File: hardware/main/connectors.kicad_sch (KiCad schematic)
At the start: 0 parts

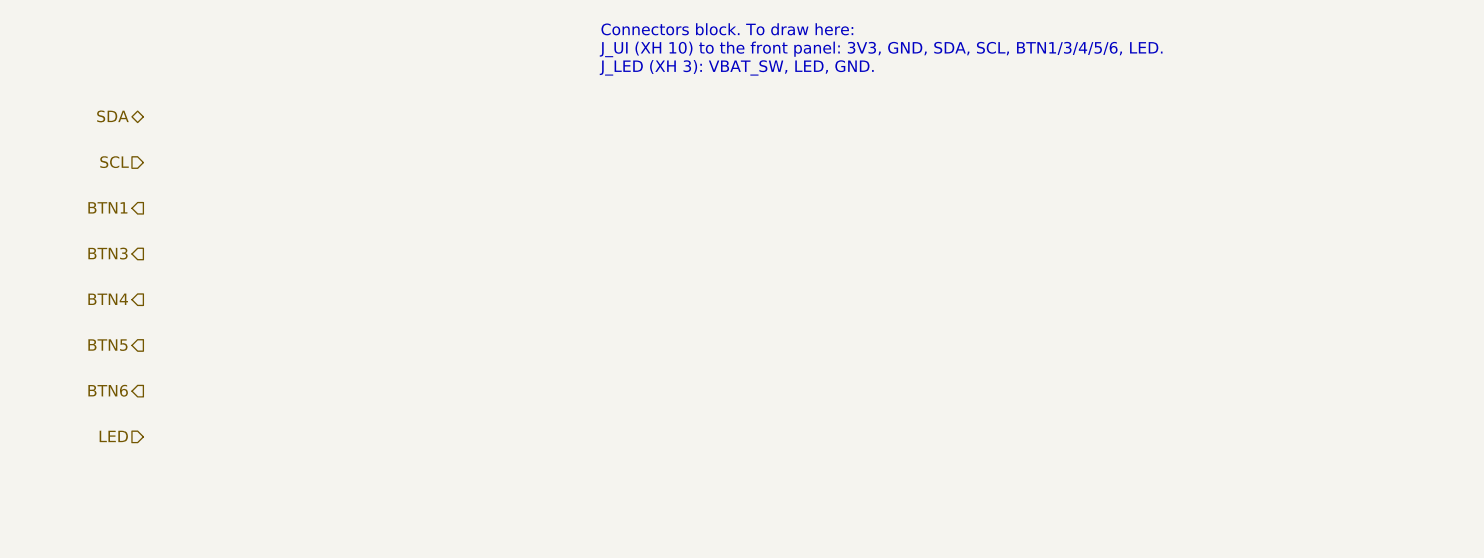
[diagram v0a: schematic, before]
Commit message: hardware: footprints for every part, LCSC library, real A1S pin plan
- lib/lcsc: ESP32-A1S, NS4150B, FS8205A, MSK12C02, PJ-320D imported
  from LCSC with easyeda2kicad (3D paths fixed, NPTH pegs, A1S antenna
  keepout and courtyard), registered in all three projects.
- Parts table with footprint and LCSC number in hardware/README.md.
- The A1S keeps the codec's I2C/I2S inside: display moves to the
  ST7789's pins 14/13/15/22 (SPI or I2C), LED to 12, CHRG/STDBY to 4/2
  through BAT54W. J_SW and J_CHG for an off-board switch and charge LEDs.
- Block sheets use the module's real outputs (HPOUTL/R, SPOLP/N, SPORP/N).

Co-Authored-By: Claude Opus 5.5 <noreply@anthropic.com>
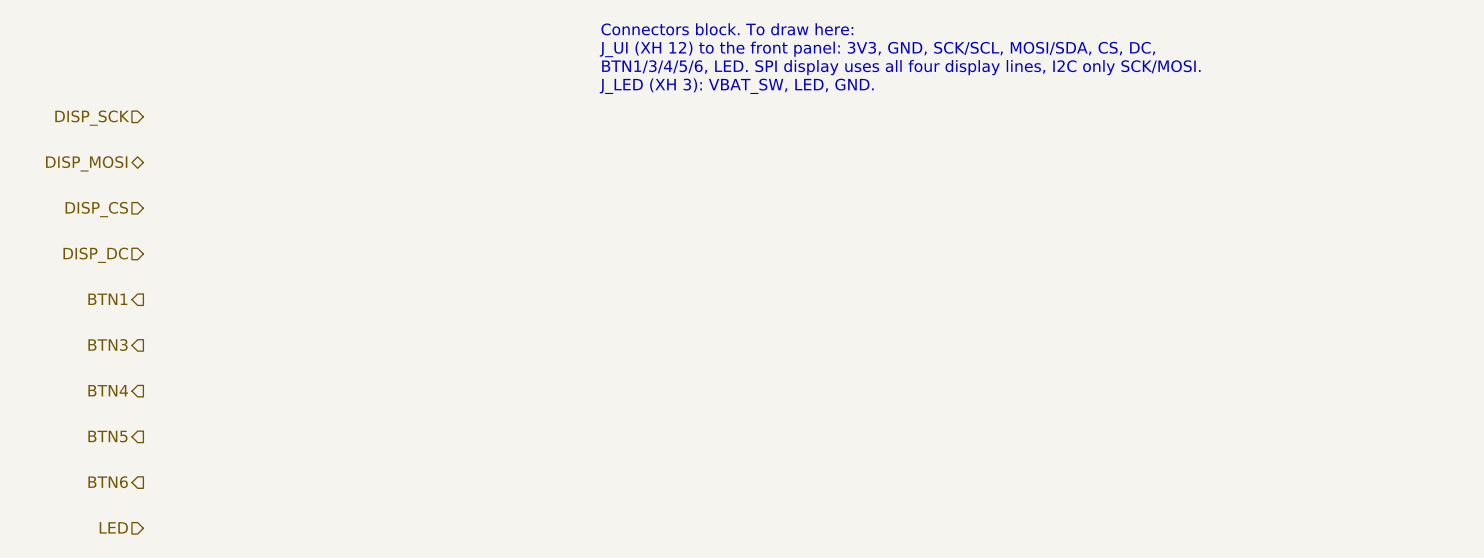
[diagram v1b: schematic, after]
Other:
- note added: "Connectors block. To draw here: J_UI (XH 12) to the front panel: 3V3, GND, SCK/SCL, MOSI/SDA, CS, DC, BTN1/3/4/5/6, LED. SPI display uses all four display lines, I2C only SCK/MOSI. J_LED (XH 3): VBAT_SW, LED, GND."
- note removed: "Connectors block. To draw here: J_UI (XH 10) to the front panel: 3V3, GND, SDA, SCL, BTN1/3/4/5/6, LED. J_LED (XH 3): VBAT_SW, LED, GND."
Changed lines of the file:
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@@
 		(rev "A")
 	)
-	(text "Connectors block. To draw here:\nJ_UI (XH 10) to the front panel: 3V3, GND, SDA, SCL, BTN1/3/4/5/6, LED.\nJ_LED (XH 3): VBAT_SW, LED, GND."
+	(text "Connectors block. To draw here:\nJ_UI (XH 12) to the front panel: 3V3, GND, SCK/SCL, MOSI/SDA, CS, DC,\nBTN1/3/4/5/6, LED. SPI display uses all four display lines, I2C only SCK/MOSI.\nJ_LED (XH 3): VBAT_SW, LED, GND."
 		(exclude_from_sim no)
 		(at 101.6 40.64 0)
@@
 		)
 	)
-	(hierarchical_label "BTN4"
+	(hierarchical_label "DISP_MOSI"
+		(shape bidirectional)
+		(at 50.8 55.88 180)
+		(effects
+			(font
+				(size 1.27 1.27)
+			)
+			(justify right)
+		)
+	)
+	(hierarchical_label "LED"
+		(shape input)
+		(at 50.8 96.52 180)
+		(effects
+			(font
+				(size 1.27 1.27)
+			)
+			(justify right)
+		)
+	)
+	(hierarchical_label "DISP_DC"
+		(shape input)
+		(at 50.8 66.04 180)
+		(effects
+			(font
+				(size 1.27 1.27)
+			)
+			(justify right)
+		)
+	)
+	(hierarchical_label "BTN6"
 		(shape output)
-		(at 50.8 71.12 180)
+		(at 50.8 91.44 180)
 		(effects
 			(font
@@
 	(hierarchical_label "BTN3"
 		(shape output)
-		(at 50.8 66.04 180)
-		(effects
-			(font
-				(size 1.27 1.27)
-			)
-			(justify right)
-		)
-	)
-	(hierarchical_label "SDA"
-		(shape bidirectional)
-		(at 50.8 50.8 180)
+		(at 50.8 76.2 180)
 		(effects
 			(font
@@
 	(hierarchical_label "BTN5"
 		(shape output)
-		(at 50.8 76.2 180)
+		(at 50.8 86.36 180)
+		(effects
+			(font
+				(size 1.27 1.27)
+			)
+			(justify right)
+		)
+	)
+	(hierarchical_label "DISP_CS"
+		(shape input)
+		(at 50.8 60.96 180)
+		(effects
+			(font
+				(size 1.27 1.27)
+			)
+			(justify right)
+		)
+	)
+	(hierarchical_label "DISP_SCK"
+		(shape input)
+		(at 50.8 50.8 180)
+		(effects
+			(font
+				(size 1.27 1.27)
+			)
+			(justify right)
+		)
+	)
+	(hierarchical_label "BTN4"
+		(shape output)
+		(at 50.8 81.28 180)
 		(effects
 			(font
@@
 	(hierarchical_label "BTN1"
 		(shape output)
-		(at 50.8 60.96 180)
+		(at 50.8 71.12 180)
 		(effects
 			(font
-				(size 1.27 1.27)
-			)
-			(justify right)
-		)
-	)
-	(hierarchical_label "SCL"
-		(shape input)
-		(at 50.8 55.88 180)
-		(effects
-			(font
-				(size 1.27 1.27)
-			)
-			(justify right)
-		)
-	)
-	(hierarchical_label "BTN6"
-		(shape output)
-		(at 50.8 81.28 180)
-		(effects
-			(font
-				(size 1.27 1.27)
-			)
-			(justify right)
-		)
-	)
-	(hierarchical_label "LED"
-		(shape input)
-		(at 50.8 86.36 180)
-		(effects
-			(font

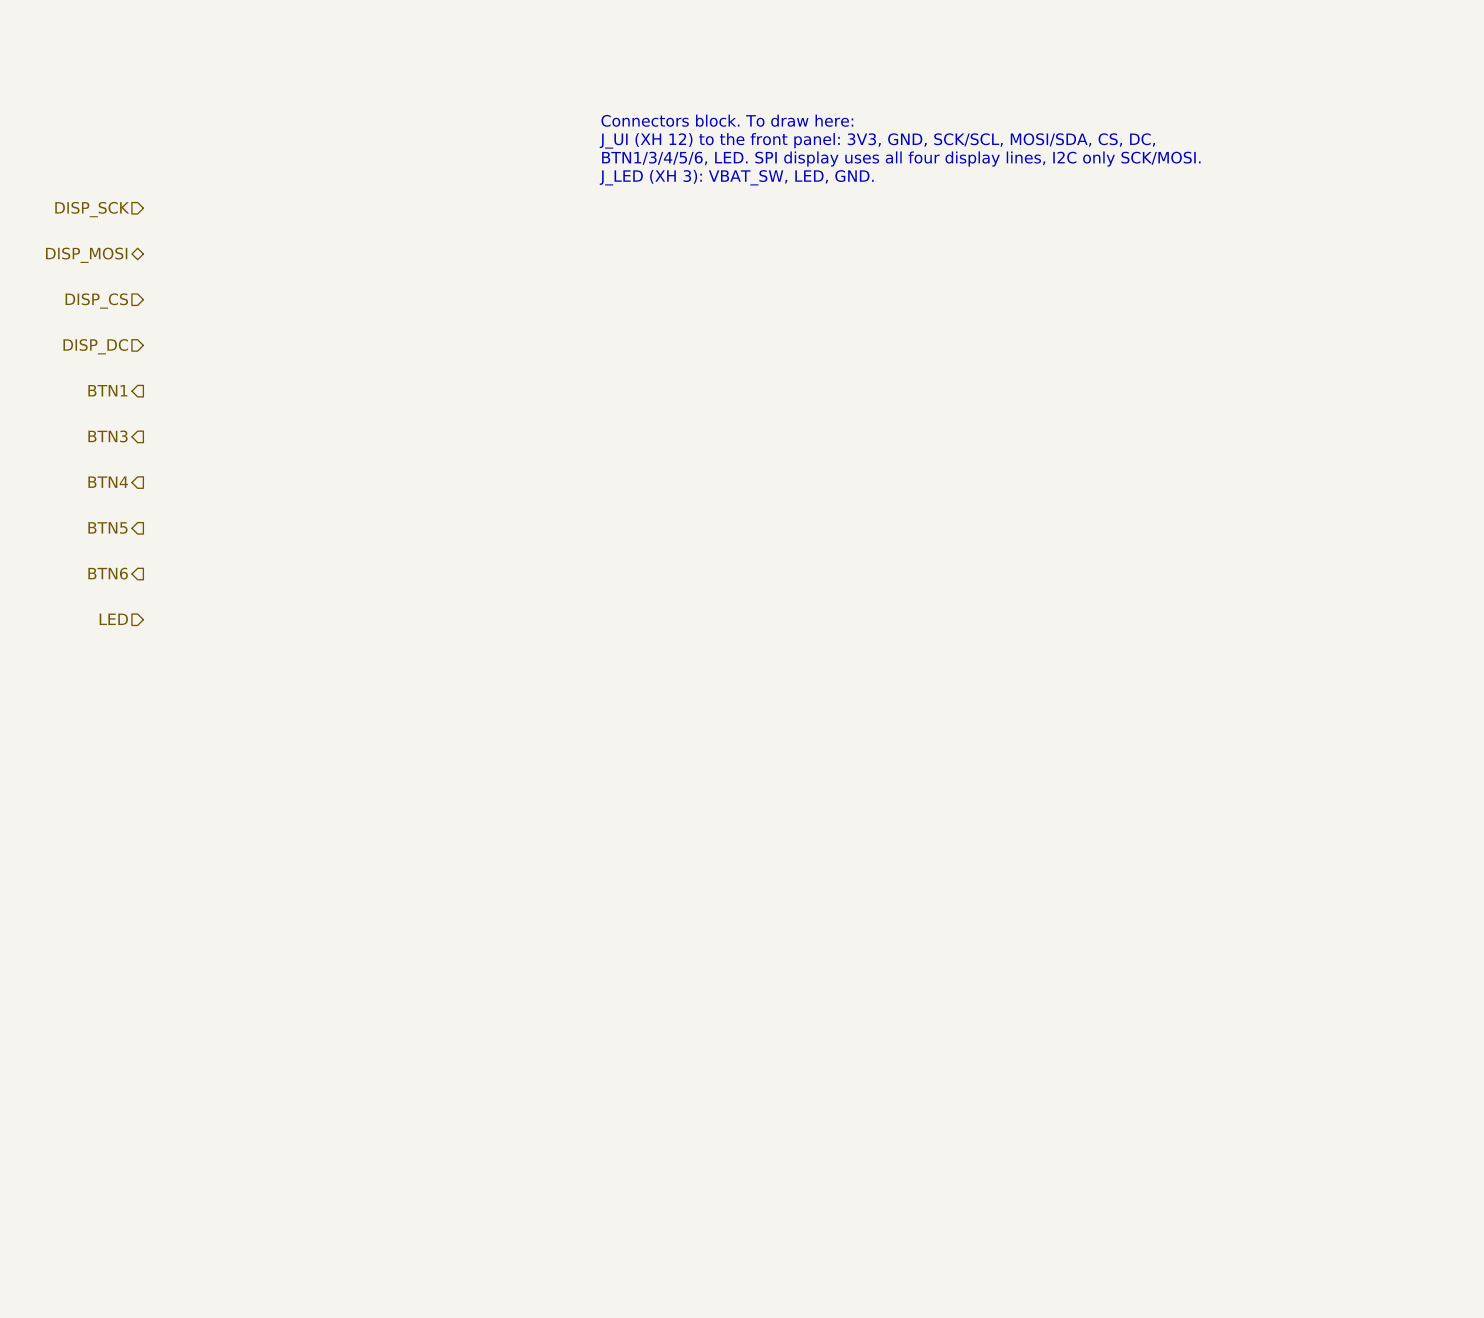
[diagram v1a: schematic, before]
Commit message: hardware: USB, Audio and Connectors sheets; main board ERC clean
Co-Authored-By: Claude Opus 5.5 <noreply@anthropic.com>
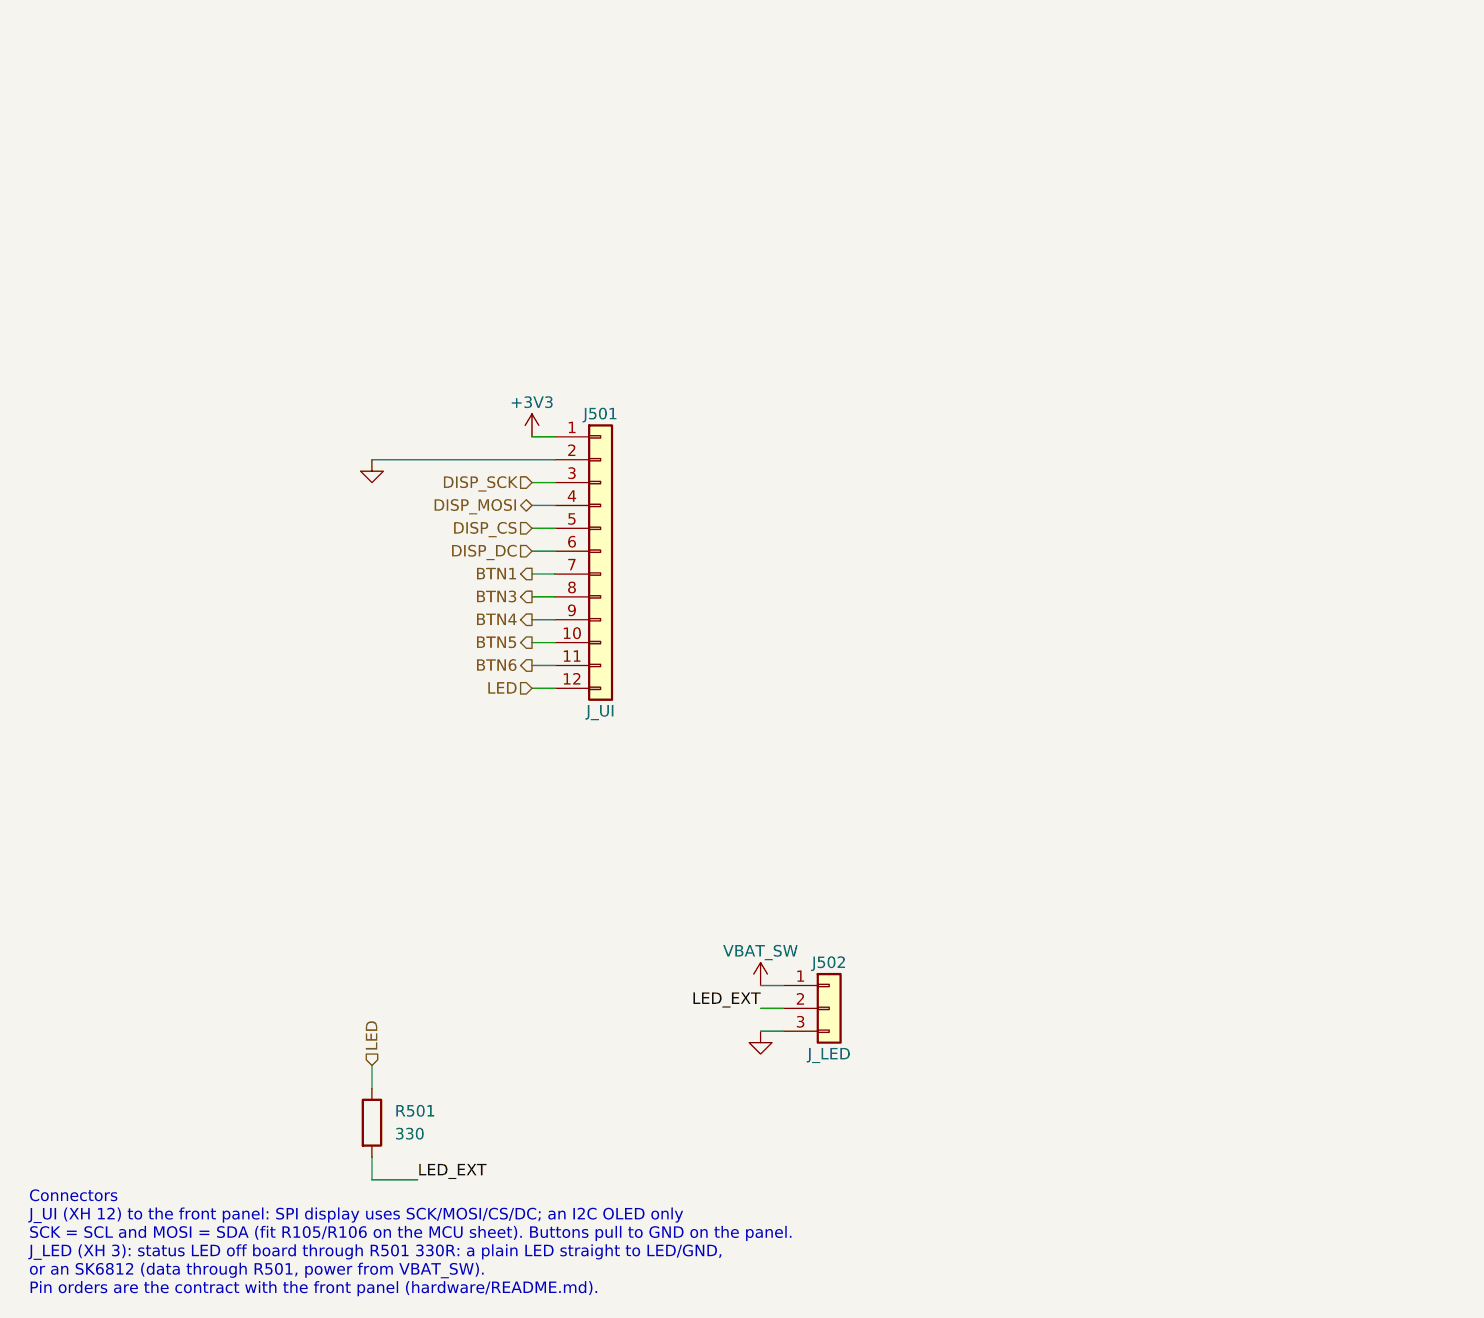
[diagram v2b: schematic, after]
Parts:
- added J501: J_UI, Connector_JST:JST_XH_B12B-XH-A_1x12_P2.50mm_Vertical, symbol Connector_Generic:Conn_01x12
- added J502: J_LED, Connector_JST:JST_XH_B3B-XH-A_1x03_P2.50mm_Vertical, symbol Connector_Generic:Conn_01x03
- added R501: 330, Resistor_SMD:R_0805_2012Metric, symbol Device:R
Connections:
- net BTN1: now also J501.7 (Pin_7)
- net BTN3: now also J501.8 (Pin_8)
- net BTN4: now also J501.9 (Pin_9)
- net BTN5: now also J501.10 (Pin_10)
- net BTN6: now also J501.11 (Pin_11)
- net DISP_CS: now also J501.5 (Pin_5)
- net DISP_DC: now also J501.6 (Pin_6)
- net DISP_MOSI: now also J501.4 (Pin_4)
- net DISP_SCK: now also J501.3 (Pin_3)
- net LED: now also J501.12 (Pin_12), R501.1
- new net +3V3: J501.1 (Pin_1)
- new net GND: J501.2 (Pin_2), J502.3 (Pin_3)
- new net LED_EXT: J502.2 (Pin_2), R501.2
- new net VBAT_SW: J502.1 (Pin_1)
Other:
- note added: "Connectors J_UI (XH 12) to the front panel: SPI display uses SCK/MOSI/CS/DC; an I2C OLED only SCK = SCL and MOSI = SDA (fit R105/R106 on the MCU sheet). Buttons pull to GND on the panel. J_LED (XH 3): status LED off board through R501 330R: a plain LED straight to LED/GND, or an SK6812 (data through R501, power from VBAT_SW). Pin orders are the contract with the front panel (hardware/README.md)."
- note removed: "Connectors block. To draw here: J_UI (XH 12) to the front panel: 3V3, GND, SCK/SCL, MOSI/SDA, CS, DC, BTN1/3/4/5/6, LED. SPI display uses all four display lines, I2C only SCK/MOSI. J_LED (XH 3): VBAT_SW, LED, GND."
